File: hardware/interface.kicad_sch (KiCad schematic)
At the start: 18 parts, among them P1 TS2068_Edge, SW1 TS Reset, SW2 NMI, U1 74LVC245APW, U2 74LVC245APW, U3 74LVC245APW, U4 74LVC245APW, U6 74LVC32APW, U7 74LVC06AD

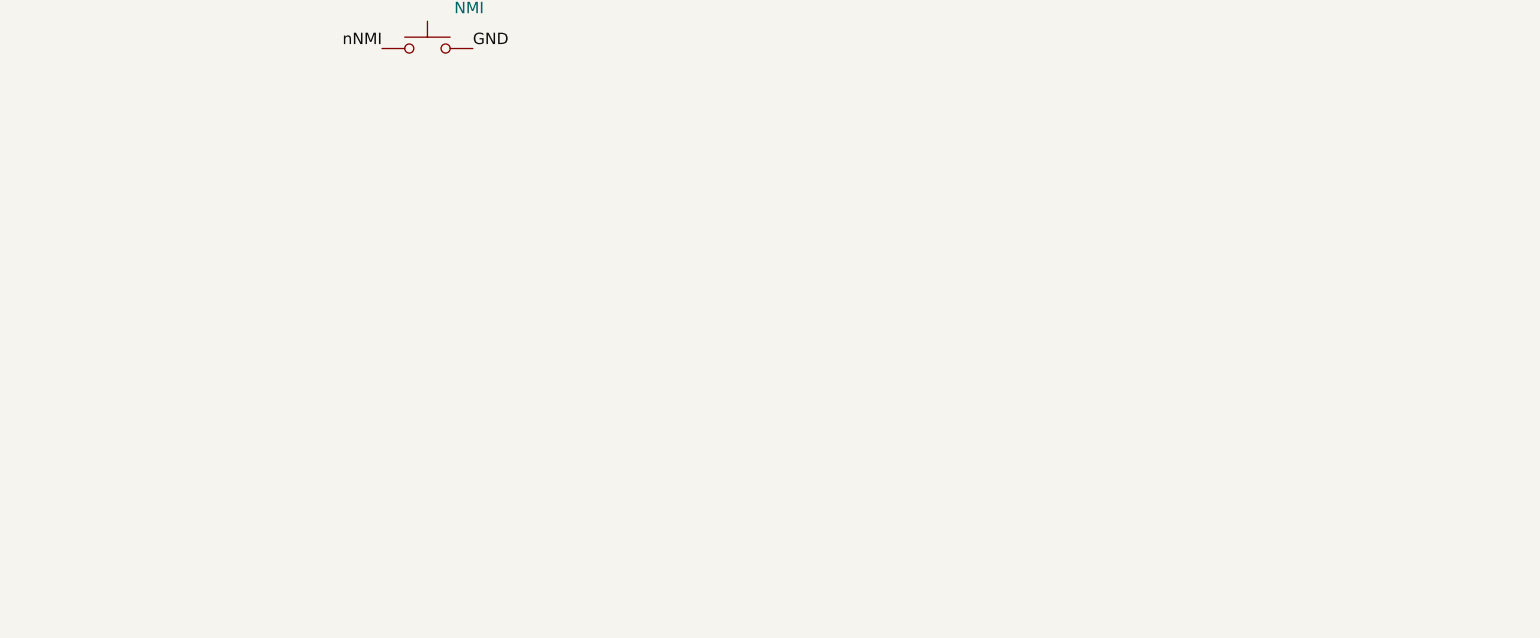
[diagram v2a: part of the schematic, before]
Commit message: v3 prototype 2: bus pull-ups, SD socket power switch, PSRAM footprint
Fixes from proto1 bring-up and issue #21:

- R14 2k2 from nBE (edge A29) to +5V_EDGE. The 74LVC06 only pulls /BE
  low; without a pull-up it rose too slowly and a RAM opcode fetch after
  a served byte read wrong bits. Same value as the bodge on board 1.
- R15-R17 10k pull-ups on GP8-GP10 (nAEN_LO, nAEN_HI, nDATA_OE). The
  RP2350 resets its pads with pull-downs, so in reset and BOOTSEL all
  three buffers were enabled and U1 and U2 both drove MD.
- U32 SY6280AAC current-limited switch on the SD socket's VDD (+3V3_SD),
  enabled from XL9555 P0.6 (SD_PWR_EN), held off by R43 until the
  firmware sets it; R42 15k sets 0.45 A. A card that latches up hits the
  limit instead of pulling +3V3 down and resetting the RP2350B, and a
  wedged card can be power-cycled. R34-R37 move to +3V3_SD so they cannot
  power a switched-off card; the detect pull-up R38 stays on +3V3.
  Firmware: power on after the detect switch reads a card and before any
  SPI; release the SD pins before powering off.
- U22 footprint SOIC-8 3.9 x 4.9 mm. The APS6404L-3SQR-SN is SOP-8
  150 mil (AP Memory package code SN); proto1 had the 208 mil footprint.
  Still DNP; ESP-PSRAM64H (Adafruit 4677) fits the same pads by hand.

Routed by flow.py on the first attempt, DRC clean at every severity
(2119 segments, 385 vias). ERC: the one pre-existing U4 warning only.
$14.90/board at 10 with fees. PSRAM options surveyed in
docs/bom-cost-optimization.md.

Co-Authored-By: Claude Opus 5.5 <noreply@anthropic.com>
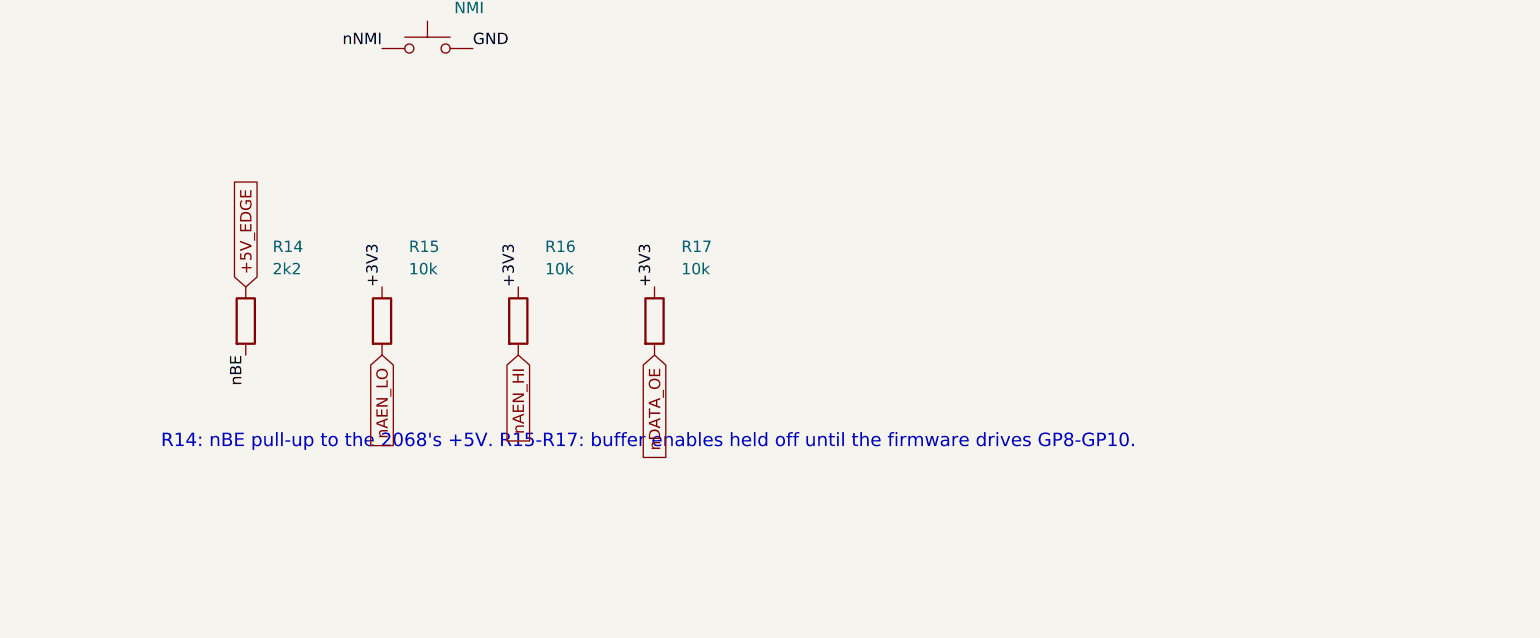
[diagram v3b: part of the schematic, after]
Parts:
- added R14: 2k2, Resistor_SMD:R_0603_1608Metric, symbol Device:R
- added R15, R16, R17: 10k, Resistor_SMD:R_0603_1608Metric, symbol Device:R
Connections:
- net +3V3: now also R15.1, R16.1, R17.1
- net +5V_EDGE: now also R14.1
- net nAEN_HI: now also R16.2
- net nAEN_LO: now also R15.2
- net nBE: now also R14.2
- net nDATA_OE: now also R17.2
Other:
- note added: "R14: nBE pull-up to the 2068's +5V. R15-R17: buffer enables held off until the firmware drives GP8-GP10."
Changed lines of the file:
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@@
   (text "R2/R3: TAPE_OUT divided to ~0.6 V for the 2068 EAR input." (exclude_from_sim no) (at 355 125 0) (effects (font (size 1.5 1.5)) (justify left bottom)))
   (text "Values to be confirmed on the prototype." (exclude_from_sim no) (at 355 128 0) (effects (font (size 1.5 1.5)) (justify left bottom)))
+  (symbol (lib_id "Device:R") (at 364.49 195.58 0) (unit 1)
+    (exclude_from_sim no) (in_bom yes) (on_board yes) (dnp no)
+    (property "Reference" "R14" (at 367.49 187.27 0) (effects (font (size 1.27 1.27)) (justify left)))
+    (property "Value" "2k2" (at 367.49 189.77 0) (effects (font (size 1.27 1.27)) (justify left)))
+    (property "Footprint" "Resistor_SMD:R_0603_1608Metric" (at 364.49 195.58 0) (effects (font (size 1.27 1.27)) (justify left) (hide yes)))
+    (property "Datasheet" "" (at 364.49 195.58 0) (effects (font (size 1.27 1.27)) (justify left) (hide yes)))
+    (property "Description" "" (at 364.49 195.58 0) (effects (font (size 1.27 1.27)) (justify left) (hide yes)))
+    (property "MPN" "0603WAF2201T5E" (at 364.49 195.58 0) (effects (font (size 1.27 1.27)) (justify left) (hide yes)))
+    (property "LCSC" "C4190" (at 364.49 195.58 0) (effects (font (size 1.27 1.27)) (justify left) (hide yes)))
+    (pin "1")
+    (pin "2")
+    (instances (project "tspico-v3" (path "/9088d141-8624-4d5c-91a9-7a3a7a90b3cc/a611a6fb-5e55-4c31-9c90-ae90d05d13a4" (reference "R14") (unit 1))))
+  )
+  (global_label "+5V_EDGE" (shape input) (at 364.49 191.77 90) (effects (font (size 1.27 1.27)) (justify left)))
+  (label "nBE" (at 364.49 199.39 270) (effects (font (size 1.27 1.27)) (justify right bottom)))
+  (symbol (lib_id "Device:R") (at 379.73 195.58 0) (unit 1)
+    (exclude_from_sim no) (in_bom yes) (on_board yes) (dnp no)
+    (property "Reference" "R15" (at 382.73 187.27 0) (effects (font (size 1.27 1.27)) (justify left)))
+    (property "Value" "10k" (at 382.73 189.77 0) (effects (font (size 1.27 1.27)) (justify left)))
+    (property "Footprint" "Resistor_SMD:R_0603_1608Metric" (at 379.73 195.58 0) (effects (font (size 1.27 1.27)) (justify left) (hide yes)))
+    (property "Datasheet" "" (at 379.73 195.58 0) (effects (font (size 1.27 1.27)) (justify left) (hide yes)))
+    (property "Description" "" (at 379.73 195.58 0) (effects (font (size 1.27 1.27)) (justify left) (hide yes)))
+    (property "MPN" "0603WAF1002T5E" (at 379.73 195.58 0) (effects (font (size 1.27 1.27)) (justify left) (hide yes)))
+    (property "LCSC" "C25804" (at 379.73 195.58 0) (effects (font (size 1.27 1.27)) (justify left) (hide yes)))
+    (pin "1")
+    (pin "2")
+    (instances (project "tspico-v3" (path "/9088d141-8624-4d5c-91a9-7a3a7a90b3cc/a611a6fb-5e55-4c31-9c90-ae90d05d13a4" (reference "R15") (unit 1))))
+  )
+  (label "+3V3" (at 379.73 191.77 90) (effects (font (size 1.27 1.27)) (justify left bottom)))
+  (global_label "nAEN_LO" (shape input) (at 379.73 199.39 270) (effects (font (size 1.27 1.27)) (justify right)))
+  (symbol (lib_id "Device:R") (at 394.97 195.58 0) (unit 1)
+    (exclude_from_sim no) (in_bom yes) (on_board yes) (dnp no)
+    (property "Reference" "R16" (at 397.97 187.27 0) (effects (font (size 1.27 1.27)) (justify left)))
+    (property "Value" "10k" (at 397.97 189.77 0) (effects (font (size 1.27 1.27)) (justify left)))
+    (property "Footprint" "Resistor_SMD:R_0603_1608Metric" (at 394.97 195.58 0) (effects (font (size 1.27 1.27)) (justify left) (hide yes)))
+    (property "Datasheet" "" (at 394.97 195.58 0) (effects (font (size 1.27 1.27)) (justify left) (hide yes)))
+    (property "Description" "" (at 394.97 195.58 0) (effects (font (size 1.27 1.27)) (justify left) (hide yes)))
+    (property "MPN" "0603WAF1002T5E" (at 394.97 195.58 0) (effects (font (size 1.27 1.27)) (justify left) (hide yes)))
+    (property "LCSC" "C25804" (at 394.97 195.58 0) (effects (font (size 1.27 1.27)) (justify left) (hide yes)))
+    (pin "1")
+    (pin "2")
+    (instances (project "tspico-v3" (path "/9088d141-8624-4d5c-91a9-7a3a7a90b3cc/a611a6fb-5e55-4c31-9c90-ae90d05d13a4" (reference "R16") (unit 1))))
+  )
+  (label "+3V3" (at 394.97 191.77 90) (effects (font (size 1.27 1.27)) (justify left bottom)))
+  (global_label "nAEN_HI" (shape input) (at 394.97 199.39 270) (effects (font (size 1.27 1.27)) (justify right)))
+  (symbol (lib_id "Device:R") (at 410.21 195.58 0) (unit 1)
+    (exclude_from_sim no) (in_bom yes) (on_board yes) (dnp no)
+    (property "Reference" "R17" (at 413.21 187.27 0) (effects (font (size 1.27 1.27)) (justify left)))
+    (property "Value" "10k" (at 413.21 189.77 0) (effects (font (size 1.27 1.27)) (justify left)))
+    (property "Footprint" "Resistor_SMD:R_0603_1608Metric" (at 410.21 195.58 0) (effects (font (size 1.27 1.27)) (justify left) (hide yes)))
+    (property "Datasheet" "" (at 410.21 195.58 0) (effects (font (size 1.27 1.27)) (justify left) (hide yes)))
+    (property "Description" "" (at 410.21 195.58 0) (effects (font (size 1.27 1.27)) (justify left) (hide yes)))
+    (property "MPN" "0603WAF1002T5E" (at 410.21 195.58 0) (effects (font (size 1.27 1.27)) (justify left) (hide yes)))
+    (property "LCSC" "C25804" (at 410.21 195.58 0) (effects (font (size 1.27 1.27)) (justify left) (hide yes)))
+    (pin "1")
+    (pin "2")
+    (instances (project "tspico-v3" (path "/9088d141-8624-4d5c-91a9-7a3a7a90b3cc/a611a6fb-5e55-4c31-9c90-ae90d05d13a4" (reference "R17") (unit 1))))
+  )
+  (label "+3V3" (at 410.21 191.77 90) (effects (font (size 1.27 1.27)) (justify left bottom)))
+  (global_label "nDATA_OE" (shape input) (at 410.21 199.39 270) (effects (font (size 1.27 1.27)) (justify right)))
+  (text "R14: nBE pull-up to the 2068's +5V. R15-R17: buffer enables held off until the firmware drives GP8-GP10." (exclude_from_sim no) (at 355 210 0) (effects (font (size 1.5 1.5)) (justify left bottom)))
   (symbol (lib_id "Device:C") (at 39.37 255.27 0) (unit 1)
     (exclude_from_sim no) (in_bom yes) (on_board yes) (dnp no)
